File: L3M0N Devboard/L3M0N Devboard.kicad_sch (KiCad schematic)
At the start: 33 parts, among them J1 USB_C_Receptacle_USB2.0_14P, J2 Conn_01x20, J3 Conn_01x20, J4 Conn_01x03, SW1 SW_Push, U1 MCP1700x-330xxTT, U2 RP2040, U3 W25Q16JVZPIQ TR, Y1 12 MHz

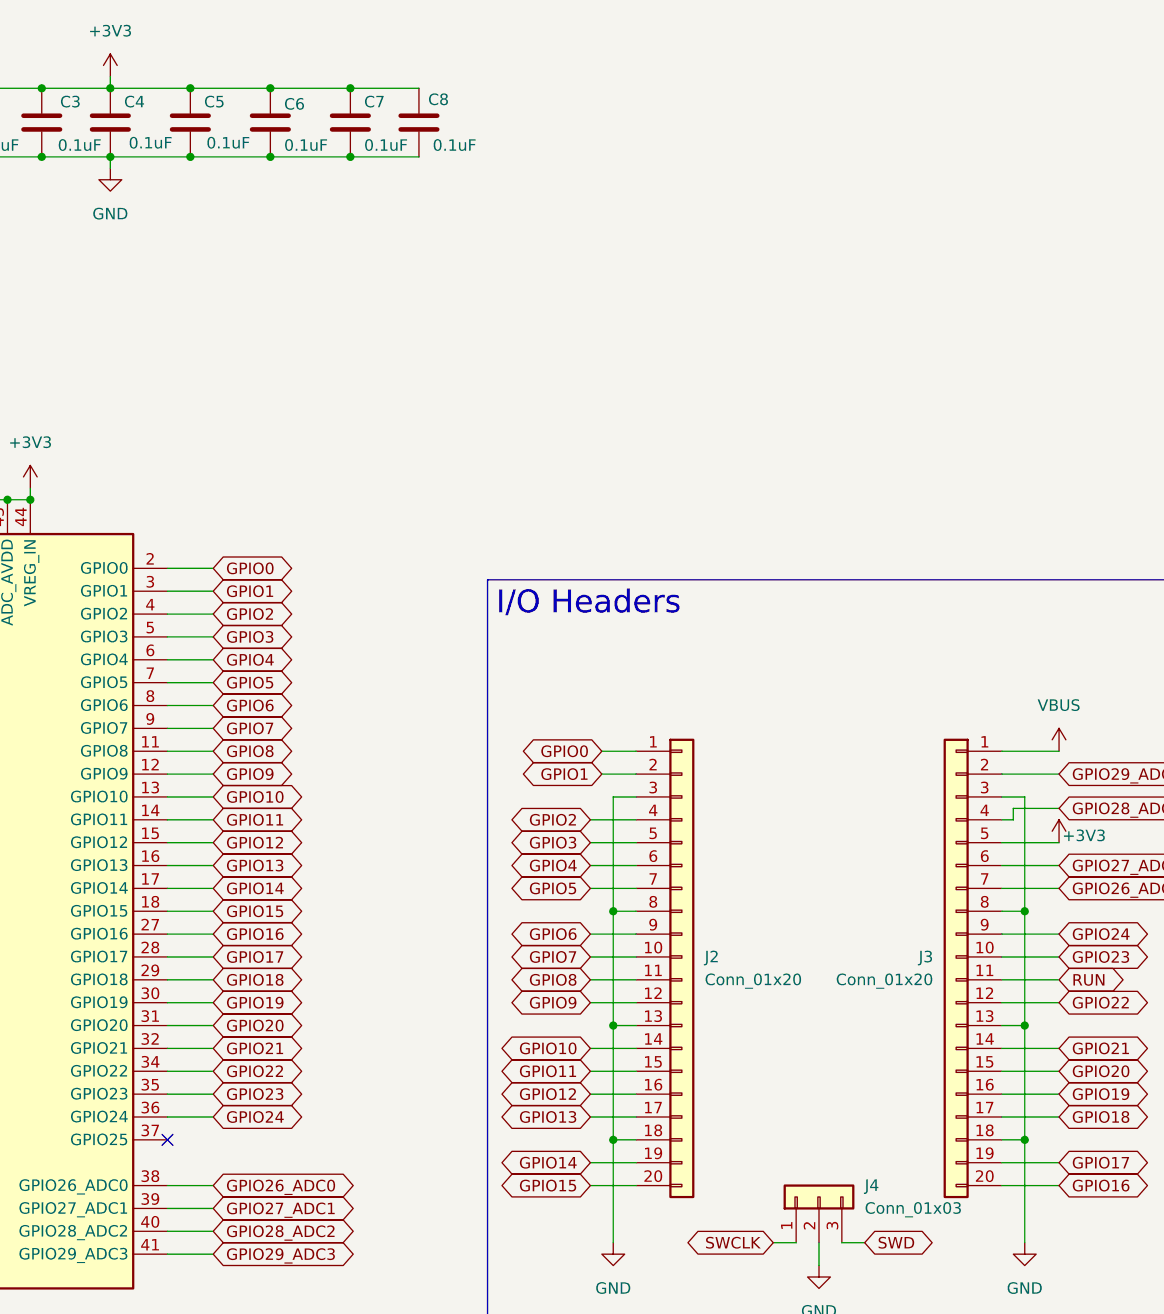
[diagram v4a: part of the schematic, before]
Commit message: Added LED and updated ReadMe
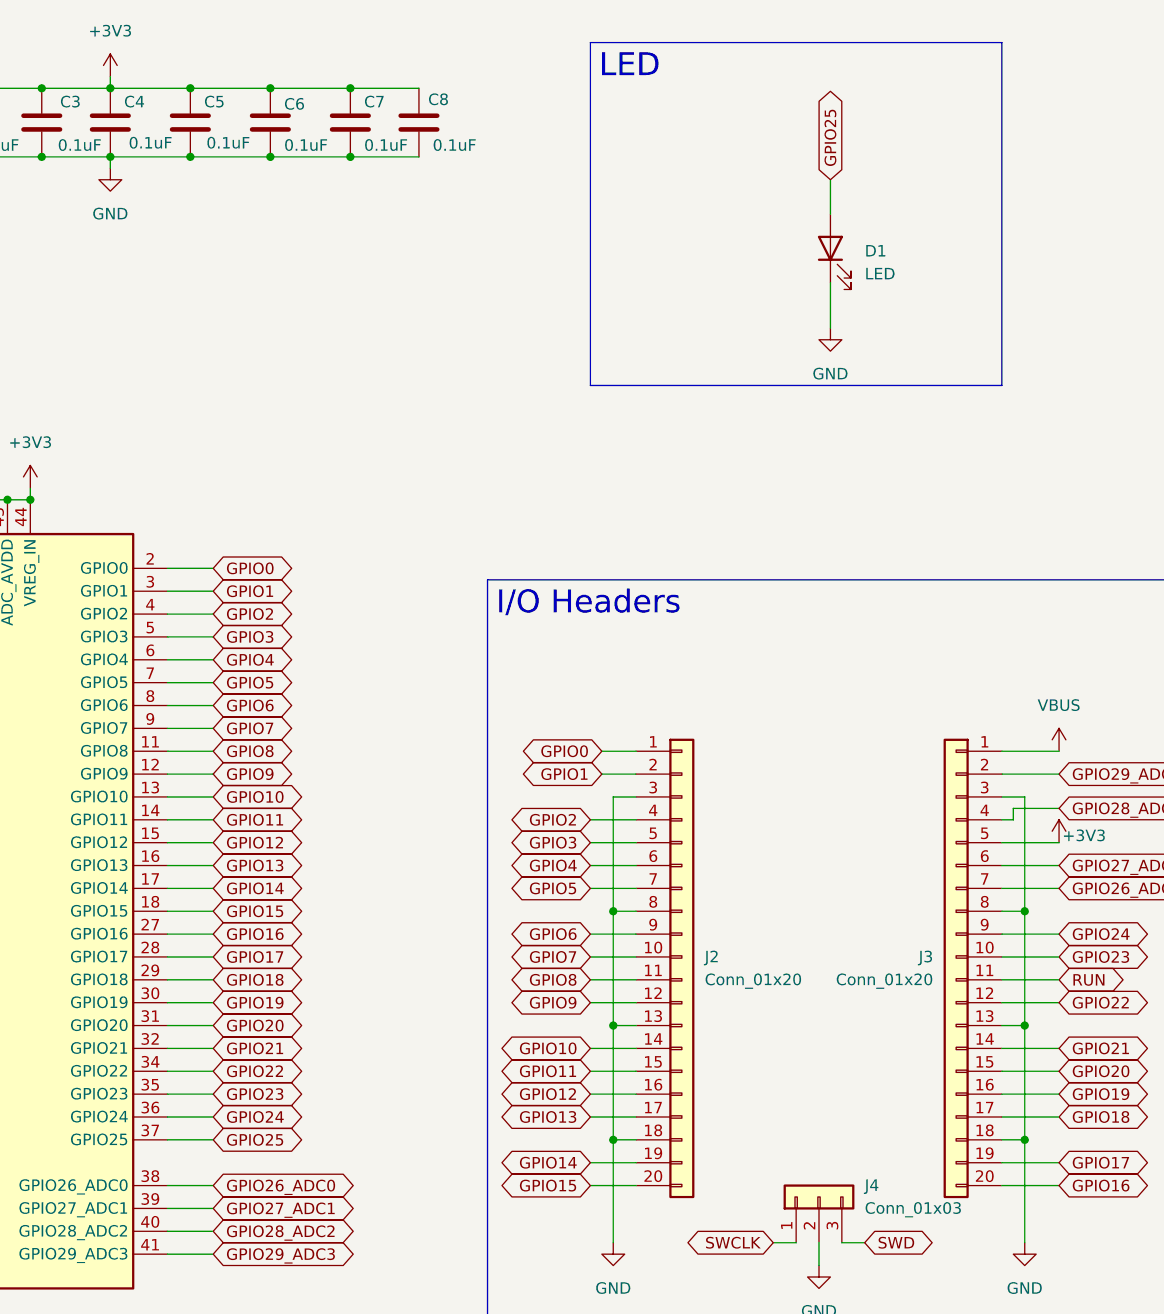
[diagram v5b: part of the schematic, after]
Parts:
- added D1: LED, LED_SMD:LED_0603_1608Metric_Pad1.05x0.95mm_HandSolder, symbol Device:LED
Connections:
- net GND: now also D1.1 (K)
- net GPIO25: now reaches U2.37 (GPIO25)
- net GPIO25: now also D1.2 (A)
- no-connect marks 1 -> 0
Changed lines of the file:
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@@
 		)
 	)
+	(text_box "LED\n"
+		(exclude_from_sim no)
+		(at 212.09 20.32 0)
+		(size 45.72 38.1)
+		(margins 0.9525 0.9525 0.9525 0.9525)
+		(stroke
+			(width 0)
+			(type solid)
+		)
+		(fill
+			(type none)
+		)
+		(effects
+			(font
+				(size 2.54 2.54)
+			)
+			(justify left top)
+		)
+	)
 	(junction
 		(at 176.53 33.02)
@@
 		(color 0 0 0 0)
 	)
-	(no_connect
-		(at 165.1 142.24)
-	)
 	(wire
 		(pts
@@
 	(wire
 		(pts
+			(xy 238.76 39.37) (xy 238.76 35.56)
+		)
+		(stroke
+			(width 0)
+			(type default)
+		)
+	)
+	(wire
+		(pts
 			(xy 54.61 34.29) (xy 62.23 34.29)
 		)
@@
 	(wire
 		(pts
+			(xy 238.76 52.07) (xy 238.76 46.99)
+		)
+		(stroke
+			(width 0)
+			(type default)
+		)
+	)
+	(wire
+		(pts
 			(xy 110.49 106.68) (xy 114.3 106.68)
 		)
@@
 	(wire
 		(pts
+			(xy 170.18 142.24) (xy 165.1 142.24)
+		)
+		(stroke
+			(width 0)
+			(type default)
+		)
+	)
+	(wire
+		(pts
 			(xy 257.81 132.08) (xy 264.16 132.08)
 		)
@@
 		)
 	)
+	(global_label "GPIO25"
+		(shape bidirectional)
+		(at 238.76 35.56 90)
+		(fields_autoplaced yes)
+		(effects
+			(font
+				(size 1.27 1.27)
+			)
+			(justify left)
+		)
+		(property "Intersheetrefs" "${INTERSHEET_REFS}"
+			(at 238.76 24.5692 90)
+			(effects
+				(font
+					(size 1.27 1.27)
+				)
+				(justify left)
+				(hide yes)
+			)
+		)
+	)
 	(global_label "GPIO7"
 		(shape bidirectional)
@@
 		)
 	)
+	(global_label "GPIO25"
+		(shape bidirectional)
+		(at 170.18 142.24 0)
+		(fields_autoplaced yes)
+		(effects
+			(font
+				(size 1.27 1.27)
+			)
+			(justify left)
+		)
+		(property "Intersheetrefs" "${INTERSHEET_REFS}"
+			(at 181.1708 142.24 0)
+			(effects
+				(font
+					(size 1.27 1.27)
+				)
+				(justify left)
+				(hide yes)
+			)
+		)
+	)
 	(global_label "GPIO14"
 		(shape bidirectional)
@@
 	)
 	(symbol
+		(lib_id "Device:LED")
+		(at 238.76 43.18 90)
+		(unit 1)
+		(exclude_from_sim no)
+		(in_bom yes)
+		(on_board yes)
+		(dnp no)
+		(fields_autoplaced yes)
+		(property "Reference" "D1"
+			(at 242.57 43.4974 90)
+			(effects
+				(font
+					(size 1.27 1.27)
+				)
+				(justify right)
+			)
+		)
+		(property "Value" "LED"
+			(at 242.57 46.0374 90)
+			(effects
+				(font
+					(size 1.27 1.27)
+				)
+				(justify right)
+			)
+		)
+		(property "Footprint" "LED_SMD:LED_0603_1608Metric_Pad1.05x0.95mm_HandSolder"
+			(at 238.76 43.18 0)
+			(effects
+				(font
+					(size 1.27 1.27)
+				)
+				(hide yes)
+			)
+		)
+		(property "Datasheet" "~"
+			(at 238.76 43.18 0)
+			(effects
+				(font
+					(size 1.27 1.27)
+				)
+				(hide yes)
+			)
+		)
+		(property "Description" "Light emitting diode"
+			(at 238.76 43.18 0)
+			(effects
+				(font
+					(size 1.27 1.27)
+				)
+				(hide yes)
+			)
+		)
+		(property "Sim.Pins" "1=K 2=A"
+			(at 238.76 43.18 0)
+			(effects
+				(font
+					(size 1.27 1.27)
+				)
+				(hide yes)
+			)
+		)
+		(pin "2"
+		)
+		(pin "1"
+		)
+		(instances
+			(project ""
+				(path "/caed3b9f-739e-408b-afa4-c258c9822a1a"
+					(reference "D1")
+					(unit 1)
+				)
+			)
+		)
+	)
+	(symbol
 		(lib_id "power:GND")
 		(at 76.2 186.69 0)
@@
 					(unit 1)
 				)
+			)
+		)
+	)
+	(symbol
+		(lib_id "power:GND")
+		(at 238.76 52.07 0)
+		(unit 1)
+		(exclude_from_sim no)
+		(in_bom yes)
+		(on_board yes)
+		(dnp no)
+		(fields_autoplaced yes)
+		(property "Reference" "#PWR027"
+			(at 238.76 58.42 0)
+			(effects
+				(font
+					(size 1.27 1.27)
+				)
+				(hide yes)
+			)
+		)
+		(property "Value" "GND"
+			(at 238.76 57.15 0)
+			(effects
+				(font
+					(size 1.27 1.27)
+				)
+			)
+		)
+		(property "Footprint" ""
+			(at 238.76 52.07 0)
+			(effects
+				(font
+					(size 1.27 1.27)
+				)
+				(hide yes)
+			)
+		)
+		(property "Datasheet" ""
+			(at 238.76 52.07 0)
+			(effects
+				(font
+					(size 1.27 1.27)
+				)
+				(hide yes)
+			)
+		)
+		(property "Description" "Power symbol creates a global label with name \"GND\" , ground"
+			(at 238.76 52.07 0)
+			(effects
+				(font
+					(size 1.27 1.27)
+				)
+				(hide yes)
+			)
+		)
+		(pin "1"
+		)
+		(instances
+			(project ""
+				(path "/caed3b9f-739e-408b-afa4-c258c9822a1a"
+					(reference "#PWR027")
+					(unit 1)
+				)
